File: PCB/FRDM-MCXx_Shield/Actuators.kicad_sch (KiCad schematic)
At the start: 2 parts, among them IC2 STPIC6C595MTR

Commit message: Updated schematic
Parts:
- removed IC2: STPIC6C595MTR, SOIC127P600X175-16N, symbol SamacSys_Parts:STPIC6C595MTR
- added C5, C6, C7: 100nF, Capacitor_SMD:C_0603_1608Metric_Pad1.08x0.95mm_HandSolder, symbol Device:C
- added D10, D11, D4, D5, D6, D7, D8, D9: LED, LED_SMD:LED_0603_1608Metric_Pad1.05x0.95mm_HandSolder, symbol Device:LED
- added D3: SK6812, LED_SMD:LED_SK6812_PLCC4_5.0x5.0mm_P3.2mm, symbol LED:SK6812
- added M1: Motor_Servo, Connector_PinHeader_2.54mm:PinHeader_1x03_P2.54mm_Vertical, symbol Motor:Motor_Servo
- added RN1, RN2: 420, Resistor_SMD:R_Array_Convex_4x0603, symbol Device:R_Pack04_Split
- added U1: STPIC6C595MTR, SOIC127P600X175-16N, symbol SamacSys_Parts:STPIC6C595MTR
- added U2: SN74LV164ADR, SOIC127P600X175-14N, symbol SamacSys_Parts:SN74LV164ADR
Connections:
- net GND: now reaches D1.1 (VSS)
- net GND: now also C5.2, C6.2, C7.2, D3.1 (VSS), M1.3 (-), RN1.1 (R1.1), RN1.2 (R2.1), RN1.3 (R3.1), RN1.4 (R4.1), RN2.1 (R1.1), RN2.2 (R2.1), RN2.3 (R3.1), RN2.4 (R4.1), U2.7 (GND)
- net LED_NEOPIXEL: now reaches D1.2 (DIN)
- net +3.3V: now reaches D1.3 (VDD)
- net +3.3V: now also C5.1, C6.1, C7.1, D3.3 (VDD), U2.14 (VCC)
- net at D1.4 (DOUT): now also D3.2 (DIN)
- new net: D5.1 (K), RN1.7 (R2.2)
- new net: D7.1 (K), RN1.5 (R4.2)
- new net: D8.1 (K), RN2.8 (R1.2)
- new net: D10.1 (K), RN2.6 (R3.2)
- new net: D4.1 (K), RN1.8 (R1.2)
- new net: D6.1 (K), RN1.6 (R3.2)
- new net: D11.1 (K), RN2.5 (R4.2)
- new net: D9.1 (K), RN2.7 (R2.2)
- new net +5V: M1.2 (+)
- new net LED_A: D4.2 (A), U2.3 (QA)
- new net LED_B: D5.2 (A), U2.4 (QB)
- new net LED_C: D6.2 (A), U2.5 (QC)
- new net LED_D: D7.2 (A), U2.6 (QD)
- new net LED_E: D8.2 (A), U2.10 (QE)
- new net LED_F: D9.2 (A), U2.11 (QF)
- new net LED_G: D10.2 (A), U2.12 (QG)
- new net LED_H: D11.2 (A), U2.13 (QH)
- new net SERVO_PWM: M1.1 (PWM)
- new net SPI_CLK: U2.8 (CLK)
- new net SPI_MOSI: U2.1 (A), U2.2 (B)
- new net ~{SPI_CS}: U2.9 (~{CLR})
- no-connect marks 0 -> 2
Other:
- company: (none) -> HAN
- title: (none) -> Actuators
- moved on the sheet: D1

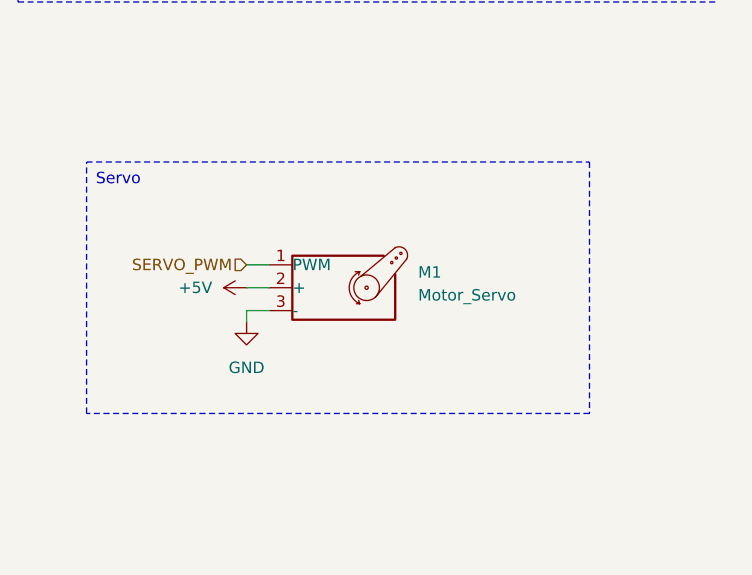
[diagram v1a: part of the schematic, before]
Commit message: Update schematic and footprint
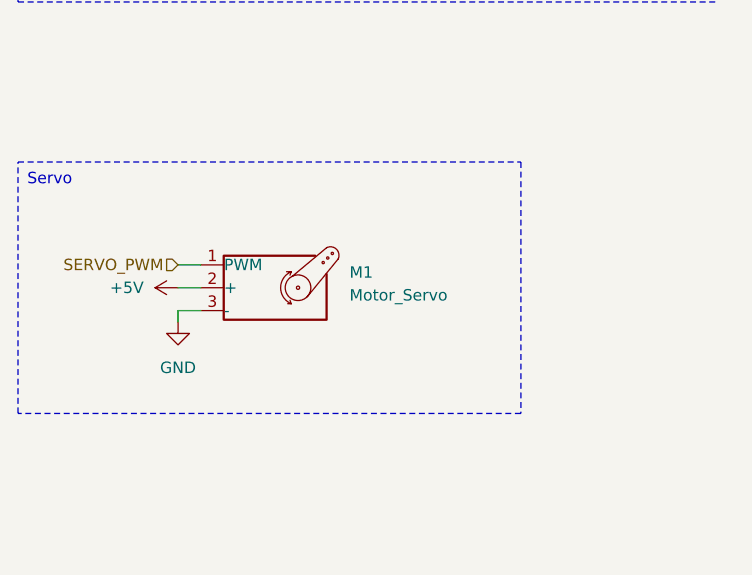
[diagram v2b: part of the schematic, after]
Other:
- moved on the sheet: M1
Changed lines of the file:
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@@
     (stroke (width 0) (type default))
   )
-  (wire (pts (xy 57.15 118.11) (xy 57.15 116.84))
+  (wire (pts (xy 49.53 118.11) (xy 49.53 116.84))
     (stroke (width 0) (type default))
   )
@@
     (stroke (width 0) (type default))
   )
-  (wire (pts (xy 57.15 111.76) (xy 59.69 111.76))
+  (wire (pts (xy 49.53 111.76) (xy 52.07 111.76))
     (stroke (width 0) (type default))
   )
@@
     (stroke (width 0) (type default))
   )
-  (wire (pts (xy 57.15 116.84) (xy 59.69 116.84))
+  (wire (pts (xy 49.53 116.84) (xy 52.07 116.84))
     (stroke (width 0) (type default))
   )
@@
     (stroke (width 0) (type default))
   )
-  (wire (pts (xy 57.15 114.3) (xy 59.69 114.3))
+  (wire (pts (xy 49.53 114.3) (xy 52.07 114.3))
     (stroke (width 0) (type default))
   )
@@
     (stroke (width 0) (type default))
   )
-  (image (at 226.06 130.81) (scale 0.201069)
+  (image (at 229.87 138.43) (scale 0.356838)
     (data
       iVBORw0KGgoAAAANSUhEUgAABj0AAASdCAIAAACU5gkAAAAAA3NCSVQICAjb4U/gAAAACXBIWXMA
@@
   )
   (text_box "Servo"
-    (at 39.37 100.33 0) (size 55.88 27.94)
+    (at 31.75 100.33 0) (size 55.88 27.94)
     (stroke (width 0) (type dash))
     (fill (type none))
@@
     (effects (font (size 1.27 1.27)) (justify left))
   )
-  (hierarchical_label "SERVO_PWM" (shape input) (at 57.15 111.76 180) (fields_autoplaced)
+  (hierarchical_label "SERVO_PWM" (shape input) (at 49.53 111.76 180) (fields_autoplaced)
     (effects (font (size 1.27 1.27)) (justify right))
   )
@@
     )
   )
-  (symbol (lib_id "power:GND") (at 57.15 118.11 0) (unit 1)
+  (symbol (lib_id "power:GND") (at 49.53 118.11 0) (unit 1)
     (in_bom yes) (on_board yes) (dnp no) (fields_autoplaced)
-    (property "Reference" "#PWR045" (at 57.15 124.46 0)
+    (property "Reference" "#PWR045" (at 49.53 124.46 0)
       (effects (font (size 1.27 1.27)) hide)
     )
-    (property "Value" "GND" (at 57.15 123.19 0)
+    (property "Value" "GND" (at 49.53 123.19 0)
       (effects (font (size 1.27 1.27)))
     )
-    (property "Footprint" "" (at 57.15 118.11 0)
+    (property "Footprint" "" (at 49.53 118.11 0)
       (effects (font (size 1.27 1.27)) hide)
     )
-    (property "Datasheet" "" (at 57.15 118.11 0)
+    (property "Datasheet" "" (at 49.53 118.11 0)
       (effects (font (size 1.27 1.27)) hide)
     )
@@
     )
   )
-  (symbol (lib_id "power:+5V") (at 57.15 114.3 90) (unit 1)
+  (symbol (lib_id "power:+5V") (at 49.53 114.3 90) (unit 1)
     (in_bom yes) (on_board yes) (dnp no) (fields_autoplaced)
-    (property "Reference" "#PWR046" (at 60.96 114.3 0)
+    (property "Reference" "#PWR046" (at 53.34 114.3 0)
       (effects (font (size 1.27 1.27)) hide)
     )
-    (property "Value" "+5V" (at 53.34 114.3 90)
+    (property "Value" "+5V" (at 45.72 114.3 90)
       (effects (font (size 1.27 1.27)) (justify left))
     )
-    (property "Footprint" "" (at 57.15 114.3 0)
+    (property "Footprint" "" (at 49.53 114.3 0)
       (effects (font (size 1.27 1.27)) hide)
     )
-    (property "Datasheet" "" (at 57.15 114.3 0)
+    (property "Datasheet" "" (at 49.53 114.3 0)
       (effects (font (size 1.27 1.27)) hide)
     )
@@
     )
   )
-  (symbol (lib_id "Motor:Motor_Servo") (at 67.31 114.3 0) (unit 1)
+  (symbol (lib_id "Motor:Motor_Servo") (at 59.69 114.3 0) (unit 1)
     (in_bom yes) (on_board yes) (dnp no)
-    (property "Reference" "M1" (at 76.2 112.5966 0)
+    (property "Reference" "M1" (at 68.58 112.5966 0)
       (effects (font (size 1.27 1.27)) (justify left))
     )
-    (property "Value" "Motor_Servo" (at 76.2 115.1366 0)
+    (property "Value" "Motor_Servo" (at 68.58 115.1366 0)
       (effects (font (size 1.27 1.27)) (justify left))
     )
-    (property "Footprint" "Connector_PinHeader_2.54mm:PinHeader_1x03_P2.54mm_Vertical" (at 67.31 119.126 0)
+    (property "Footprint" "Connector_PinHeader_2.54mm:PinHeader_1x03_P2.54mm_Vertical" (at 59.69 119.126 0)
       (effects (font (size 1.27 1.27)) hide)
     )
-    (property "Datasheet" "http://forums.parallax.com/uploads/attachments/46831/74481.png" (at 67.31 119.126 0)
+    (property "Datasheet" "http://forums.parallax.com/uploads/attachments/46831/74481.png" (at 59.69 119.126 0)
       (effects (font (size 1.27 1.27)) hide)
     )

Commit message: Updated schematic and PCB files
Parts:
- renumbered C5 to C10, C6 to C11, C7 to C12, D7 to D10, D8 to D11, D9 to D12, D10 to D13, D11 to D14, D1 to D5, D3 to D6, D4 to D7, D5 to D8, D6 to D9, RN1 to RN2, RN2 to RN3, U1 to U4, U2 to U5

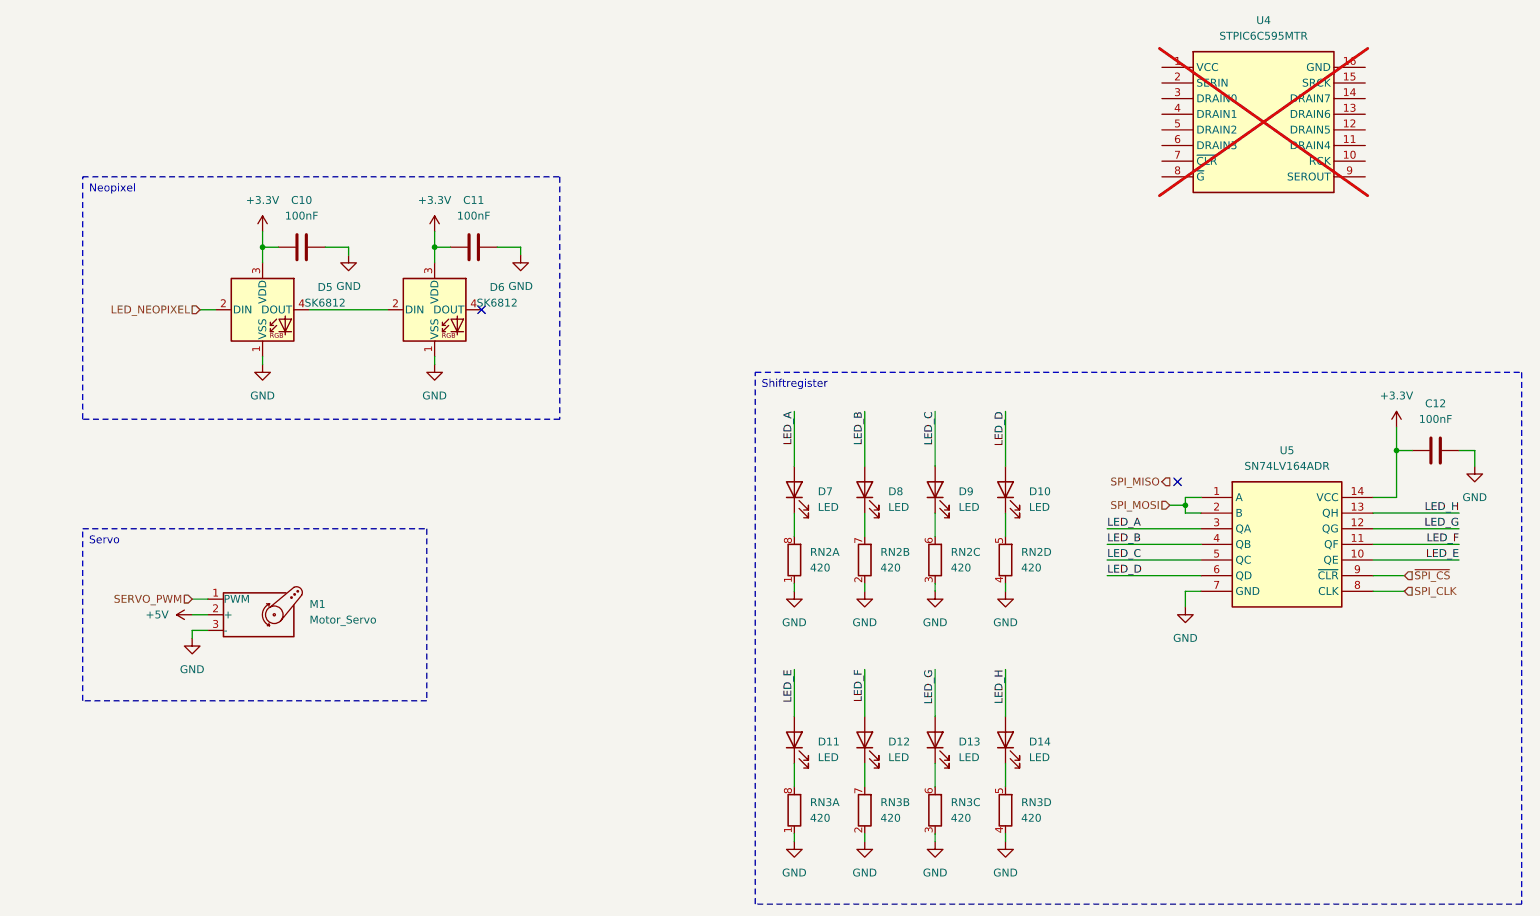
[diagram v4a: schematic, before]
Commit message: Updated schematic and PCB
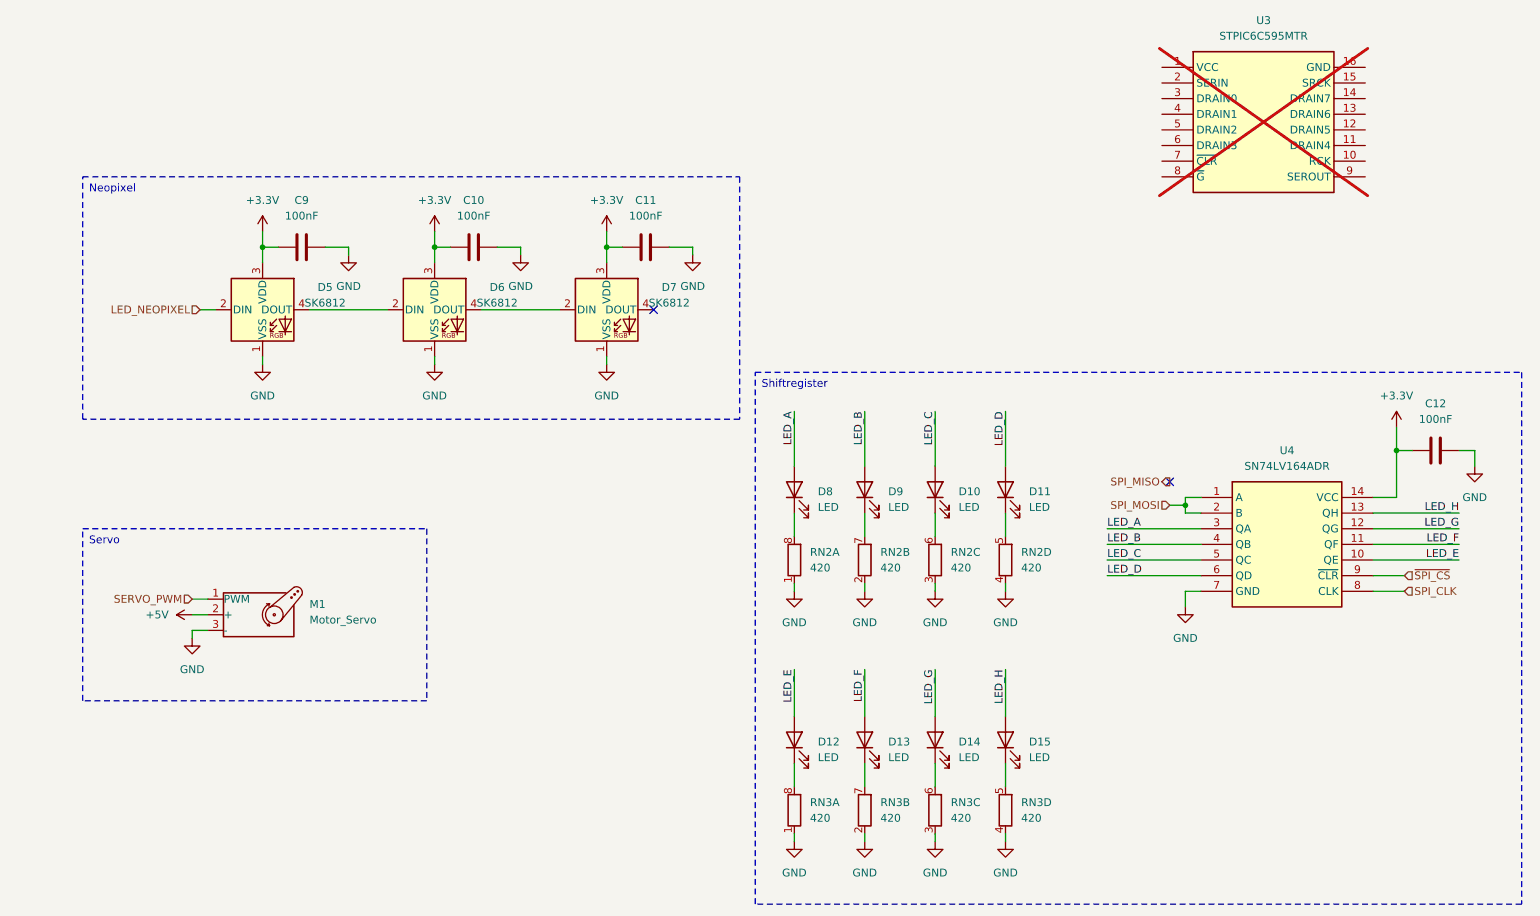
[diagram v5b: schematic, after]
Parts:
- added C11: 100nF, Capacitor_SMD:C_0603_1608Metric_Pad1.08x0.95mm_HandSolder, symbol Device:C
- added D7: SK6812, LED_SMD:LED_SK6812_PLCC4_5.0x5.0mm_P3.2mm, symbol LED:SK6812
- renumbered C11 to C10, C10 to C9, D9 to D10, D10 to D11, D11 to D12, D12 to D13, D13 to D14, D14 to D15, D7 to D8, D8 to D9, U4 to U3, U5 to U4
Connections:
- net +3.3V: now also C11.1, D7.3 (VDD)
- net GND: now also C11.2, D7.1 (VSS)
- net at D6.4 (DOUT): now also D7.2 (DIN)
